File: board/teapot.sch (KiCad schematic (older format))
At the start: 43 parts, among them P1 BATT, P2 SMA, Q1 TEPT4400, U1 TPS79333DBVR, U2 TLV61225, U3 microusb-b, U4 RFM69W, U5 STM32L052K8, U6 HTU21D, U7 MS5637, U8 SWD, Y1 32.768k

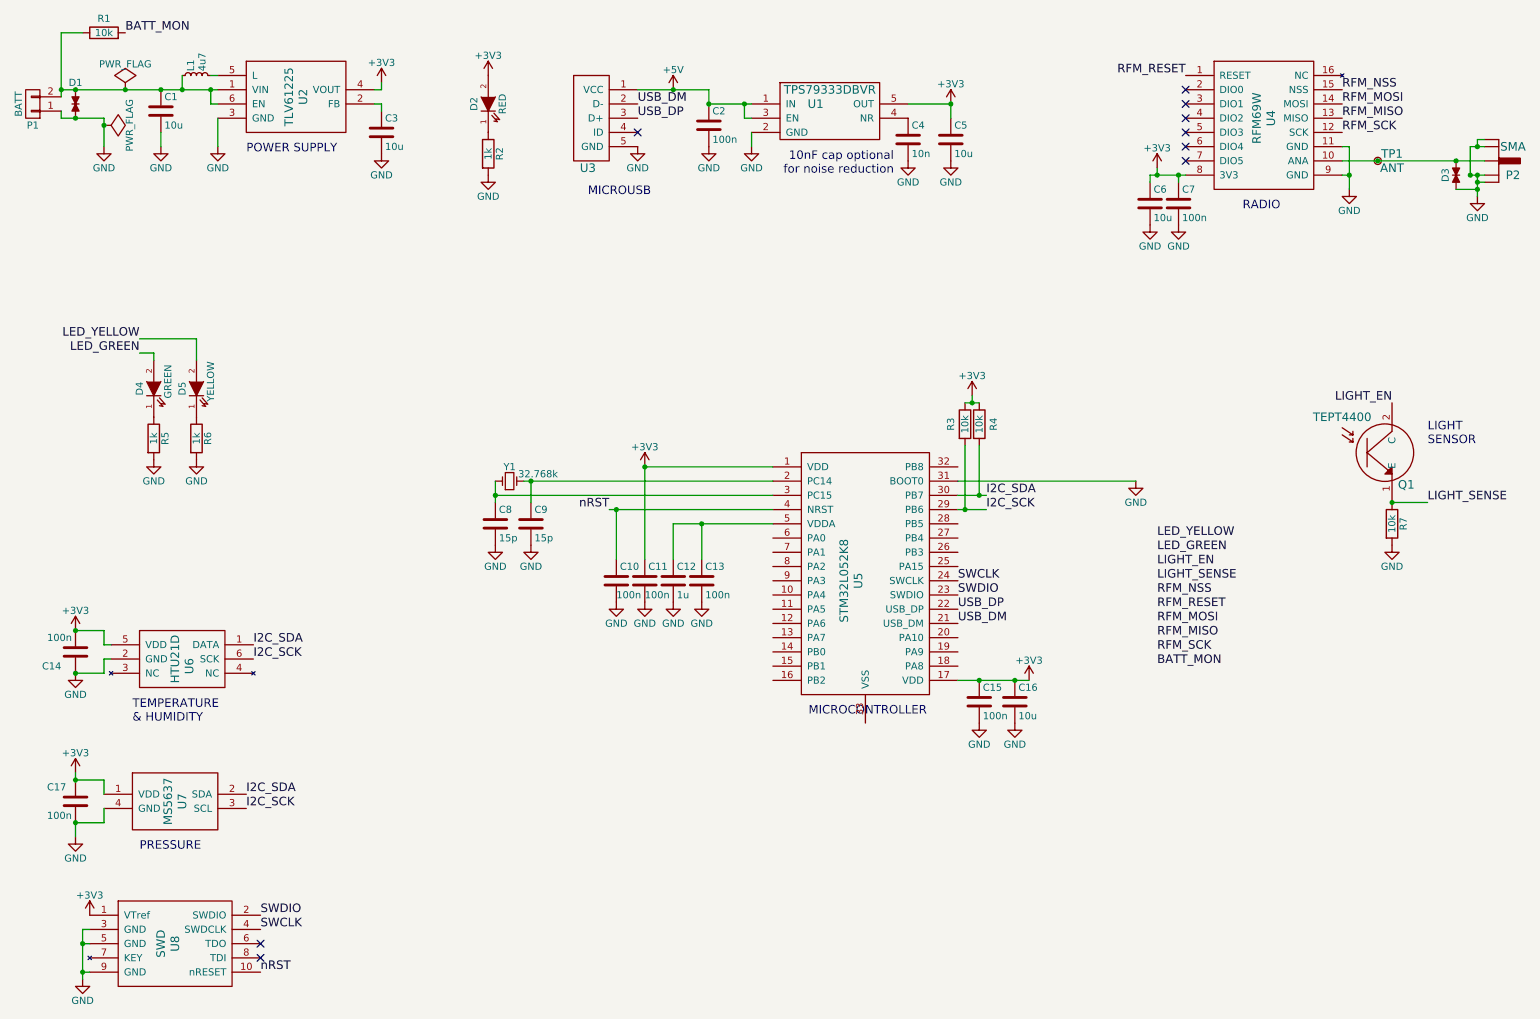
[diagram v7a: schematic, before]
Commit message: Initial placement and first successful route.
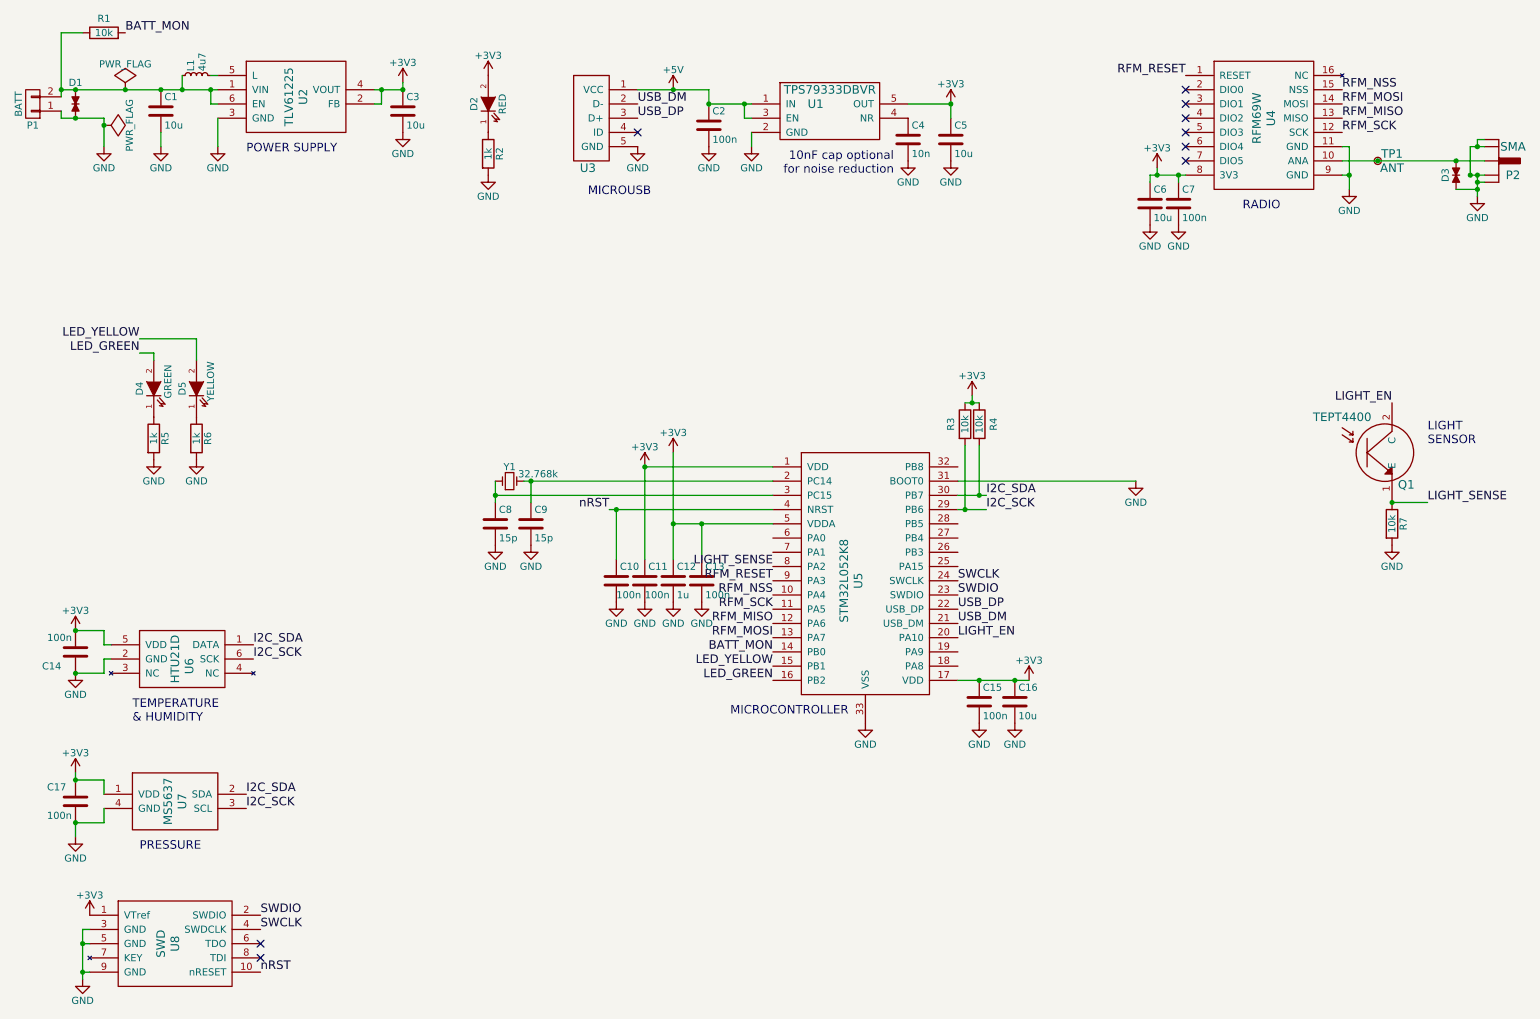
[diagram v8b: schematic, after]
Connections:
- net +3V3: now also C12.1, C13.1, C3.1, U2.2 (FB), U5.5 (VDDA)
- net BATT_MON: now also U5.14 (PB0)
- net GND: now also U5.33 (VSS)
- net LED_GREEN: now also U5.16 (PB2)
- net LED_YELLOW: now also U5.15 (PB1)
- net LIGHT_EN: now also U5.20 (PA10)
- net LIGHT_SENSE: now also U5.8 (PA2)
- net RFM_MISO: now also U5.12 (PA6)
- net RFM_MOSI: now also U5.13 (PA7)
- net RFM_NSS: now also U5.10 (PA4)
- net RFM_RESET: now also U5.9 (PA3)
- net RFM_SCK: now also U5.11 (PA5)
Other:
- moved on the sheet: C3
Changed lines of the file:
@@
 L C C3
 U 1 1 56707DD4
-P 3100 1400
-F 0 "C3" H 3125 1500 50  0000 L CNN
-F 1 "10u" H 3125 1300 50  0000 L CNN
-F 2 "Capacitors_SMD:C_0603" H 3138 1250 50  0001 C CNN
-F 3 "http://www.farnell.com/datasheets/1747457.pdf" H 3100 1400 50  0001 C CNN
-F 4 "1735528" H 3100 1400 60  0001 C CNN "Farnell"
-	1    3100 1400
+P 3250 1250
+F 0 "C3" H 3275 1350 50  0000 L CNN
+F 1 "10u" H 3275 1150 50  0000 L CNN
+F 2 "Capacitors_SMD:C_0603" H 3288 1100 50  0001 C CNN
+F 3 "http://www.farnell.com/datasheets/1747457.pdf" H 3250 1250 50  0001 C CNN
+F 4 "1735528" H 3250 1250 60  0001 C CNN "Farnell"
+	1    3250 1250
 	1    0    0    -1
 $EndComp
@@
 L GND #PWR01
 U 1 1 56707EE4
-P 3100 1550
-F 0 "#PWR01" H 3100 1300 50  0001 C CNN
-F 1 "GND" H 3100 1400 50  0000 C CNN
-F 2 "" H 3100 1550 50  0000 C CNN
-F 3 "" H 3100 1550 50  0000 C CNN
-	1    3100 1550
+P 3250 1400
+F 0 "#PWR01" H 3250 1150 50  0001 C CNN
+F 1 "GND" H 3250 1250 50  0000 C CNN
+F 2 "" H 3250 1400 50  0000 C CNN
+F 3 "" H 3250 1400 50  0000 C CNN
+	1    3250 1400
 	1    0    0    -1
 $EndComp
@@
 L +3V3 #PWR02
 U 1 1 56707F42
-P 3100 1050
-F 0 "#PWR02" H 3100 900 50  0001 C CNN
-F 1 "+3V3" H 3100 1190 50  0000 C CNN
-F 2 "" H 3100 1050 50  0000 C CNN
-F 3 "" H 3100 1050 50  0000 C CNN
-	1    3100 1050
+P 3250 1050
+F 0 "#PWR02" H 3250 900 50  0001 C CNN
+F 1 "+3V3" H 3250 1190 50  0000 C CNN
+F 2 "" H 3250 1050 50  0000 C CNN
+F 3 "" H 3250 1050 50  0000 C CNN
+	1    3250 1050
 	1    0    0    -1
 $EndComp
@@
 $EndComp
 Wire Wire Line
-	3050 1200 3100 1200
-Wire Wire Line
-	3100 1200 3100 1250
-Wire Wire Line
-	3100 1050 3100 1100
-Wire Wire Line
-	3100 1100 3050 1100
+	3050 1100 3250 1100
 Wire Wire Line
 	1950 1000 1900 1000
@@
 Text Label 7350 3950 0    60   ~ 0
 I2C_SDA
-Text Label 8550 4550 0    60   ~ 0
+Text Label 5850 4450 2    60   ~ 0
 LIGHT_SENSE
-Text Label 8550 4750 0    60   ~ 0
+Text Label 5850 4550 2    60   ~ 0
 RFM_RESET
-Text Label 8550 4650 0    60   ~ 0
+Text Label 5850 4650 2    60   ~ 0
 RFM_NSS
-Text Label 8550 5050 0    60   ~ 0
+Text Label 5850 4750 2    60   ~ 0
 RFM_SCK
-Text Label 8550 4950 0    60   ~ 0
+Text Label 5850 4850 2    60   ~ 0
 RFM_MISO
-Text Label 8550 4850 0    60   ~ 0
+Text Label 5850 4950 2    60   ~ 0
 RFM_MOSI
 $Comp
@@
 	1    0    0    -1
 $EndComp
-Text Label 8550 4250 0    60   ~ 0
+Text Label 5850 5150 2    60   ~ 0
 LED_YELLOW
-Text Label 8550 4350 0    60   ~ 0
+Text Label 5850 5250 2    60   ~ 0
 LED_GREEN
 Text Label 1400 2850 2    60   ~ 0
@@
 NoConn ~ 2250 7100
 NoConn ~ 2250 7200
-Text Notes 6100 5500 0    60   ~ 0
+Text Notes 5550 5500 0    60   ~ 0
 MICROCONTROLLER
 $Comp
@@
 	5150 4150 5850 4150
 Wire Wire Line
-	5150 4400 5150 4150
+	5150 3650 5150 4400
 Connection ~ 5350 4150
 $Comp
@@
 	10650 1800 10800 1800
 Connection ~ 10800 1800
-Text Label 8550 4450 0    60   ~ 0
+Text Label 7150 4950 0    60   ~ 0
 LIGHT_EN
 Text Label 10200 3300 2    60   ~ 0
@@
 Text Label 1300 700  0    60   ~ 0
 BATT_MON
-Text Label 8550 5150 0    60   ~ 0
+Text Label 5850 5050 2    60   ~ 0
 BATT_MON
+Connection ~ 5150 4150
+$Comp
+L +3V3 #PWR043
+U 1 1 567C63AD
+P 5150 3650
+F 0 "#PWR043" H 5150 3500 50  0001 C CNN
+F 1 "+3V3" H 5150 3790 50  0000 C CNN
+F 2 "" H 5150 3650 50  0000 C CNN
+F 3 "" H 5150 3650 50  0000 C CNN
+	1    5150 3650
+	1    0    0    -1
+$EndComp
+$Comp
+L GND #PWR044
+U 1 1 567C711D
+P 6500 5550
+F 0 "#PWR044" H 6500 5300 50  0001 C CNN
+F 1 "GND" H 6500 5400 50  0000 C CNN
+F 2 "" H 6500 5550 50  0000 C CNN
+F 3 "" H 6500 5550 50  0000 C CNN
+	1    6500 5550
+	1    0    0    -1
+$EndComp
+Wire Wire Line
+	3250 1100 3250 1050
+Connection ~ 3250 1100
+Wire Wire Line
+	3050 1200 3100 1200
+Wire Wire Line
+	3100 1200 3100 1100
+Connection ~ 3100 1100
 $EndSCHEMATC
